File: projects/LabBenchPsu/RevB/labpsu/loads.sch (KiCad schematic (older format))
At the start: 33 parts

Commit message: schematic more or less done
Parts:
- removed 100n: C, symbol C
- removed C?: 1uF, symbol C
- removed IC?: OPAMP-DUALU, SparkFun-SO08, symbol OPAMP-DUALU
- removed U?: MCP3204, symbol MCP3204
- added C19, C22, C31: 100n, symbol C
- added unit 1 of IC3
- IC2, IC3: renamed from IC?; footprint SparkFun-SO08 -> (none)
- gave numbers to parts that had none: 26
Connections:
- net 3V3Reg: now also IC2.8 (V+), C19.2, C22.2, IC3.8 (V+)
- net GND: now also IC2.4 (V-), C19.1, C22.1, C31.1, IC3.4 (V-)
- net at IC2.3 (+IN), U8.1 (VOUT): now also C31.2
- net at Q1.2 (S), R33.1, R34.1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: now also IC3.5 (+IN); no longer IC2.5 (+IN)
- net at C21.2, R42.2, R43.2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: now also IC3.3 (+IN); no longer IC3.5 (+IN)
- removed net I_LOAD: C23.2, IC2.6 (-IN), IC2.7 (OUT)
- net V_LOAD renamed I_Load
- net I_Load: now also C23.2; no longer C24.2
- new net V_Load: C24.2, IC3.1 (OUT), IC3.2 (-IN)
- no-connect marks 4 -> 3
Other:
- note added: "I_Load: \n0-2A => 0-2V"
- note added: "SetCurrent: \n0-2V => 0-2A"
- note added: "V_Load: \n0-20V => 0-2V"
- note removed: "0-2.048 V"
- note removed: "ReadVolt: 1V = 10V"
- note removed: "SetCurrent: 1V = 1A"
- moved on the sheet: C20, C24, IC2A, IC2B, IC3B, JP3, JP4, Q1, R31, R32, R35, U8

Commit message: schematic with new DAC
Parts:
- removed C22: 100n, symbol C
- removed IC2, IC3: LM324, symbol OPAMP-DUALU
- removed U8: MCP4725, symbol MCP4725
- added P10: Heatsink, symbol CONN_2
- added U11: LM324N, symbol LM324N
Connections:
- net 3V3Reg: now also U11.4 (V+)
- net GND: now also U11.11 (V-); no longer C31.1
- net I_Load: now also U11.8, U11.9 (-)
- net SetCurrent: now also C31.1, U11.5 (+)
- net V_Load: now also U11.13 (-), U11.14
- net at C31.2: now also U11.4 (V+)
- net at C20.1, R35.2: now also U11.7
- net at C20.2, R36.2: now also U11.6 (-)
- net at Q1.2 (S), R33.1, R34.1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: now also U11.10 (+)
- net at C21.2, R42.2, R43.2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: now also U11.12 (+)
- no-connect marks 3 -> 5
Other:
- note added: "Voltage divider (/10) \nand lowpass filter"
- moved on the sheet: C19, C20, C21, C23, C24, C31, JP3, JP4, P8, Q1, R31, R32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

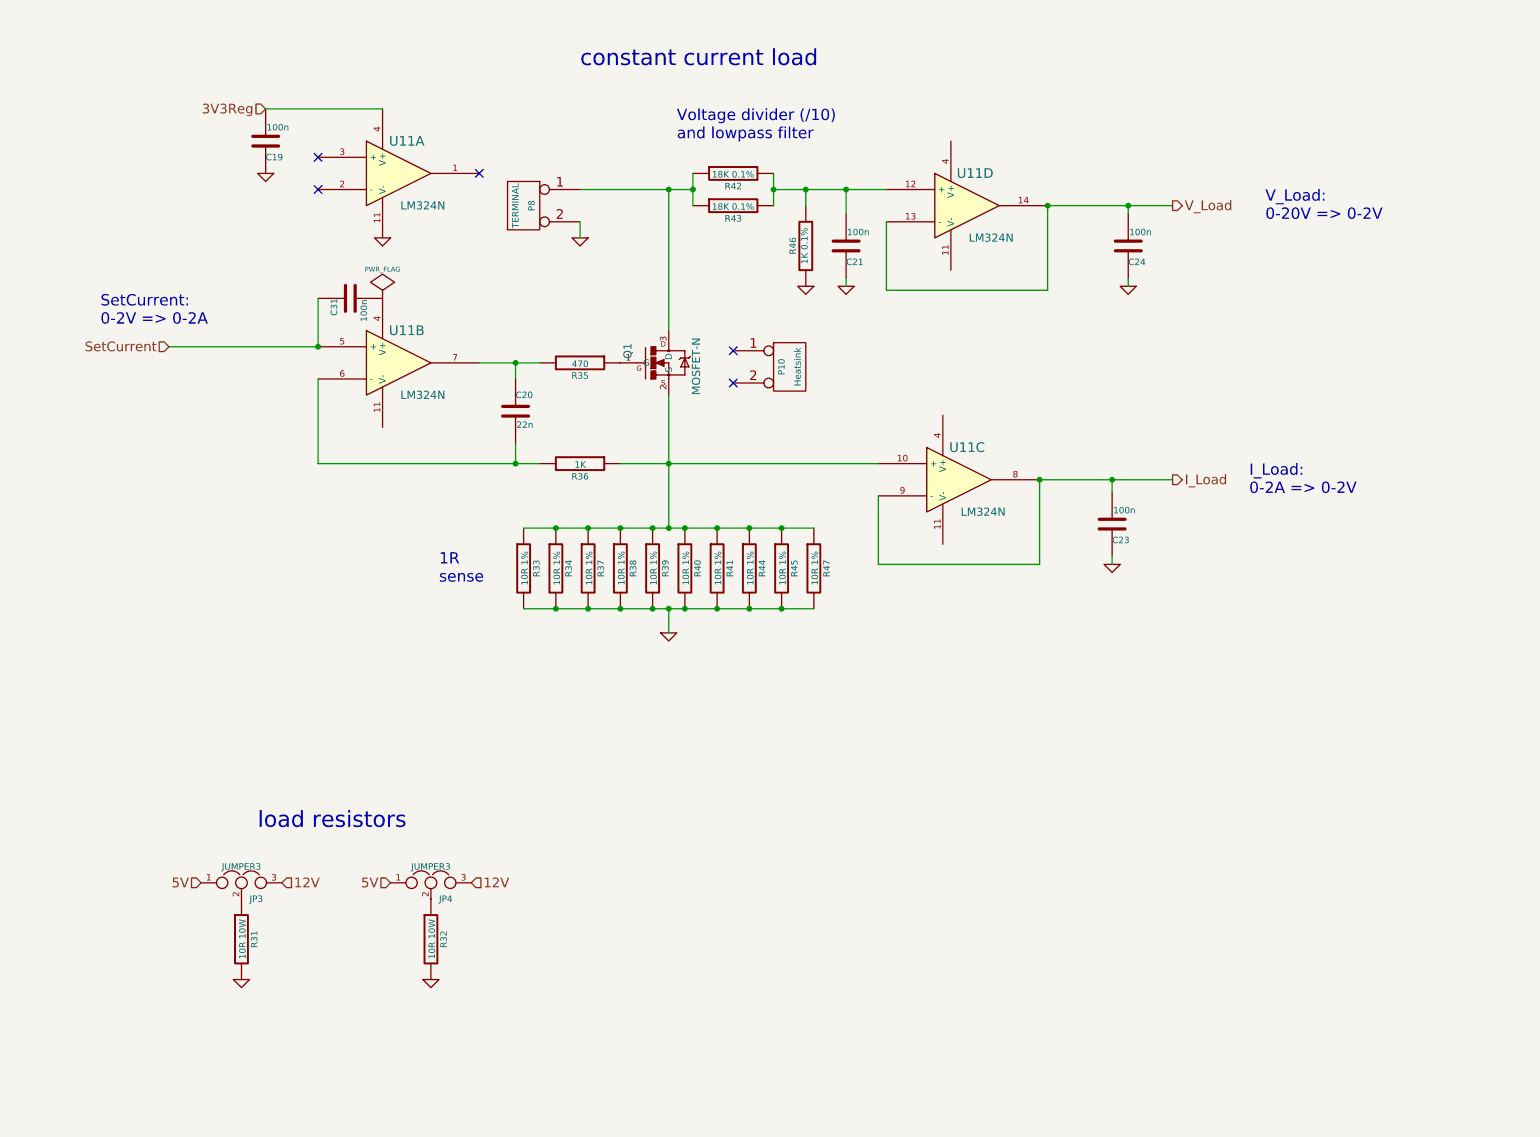
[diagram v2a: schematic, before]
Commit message: i2c addresses added
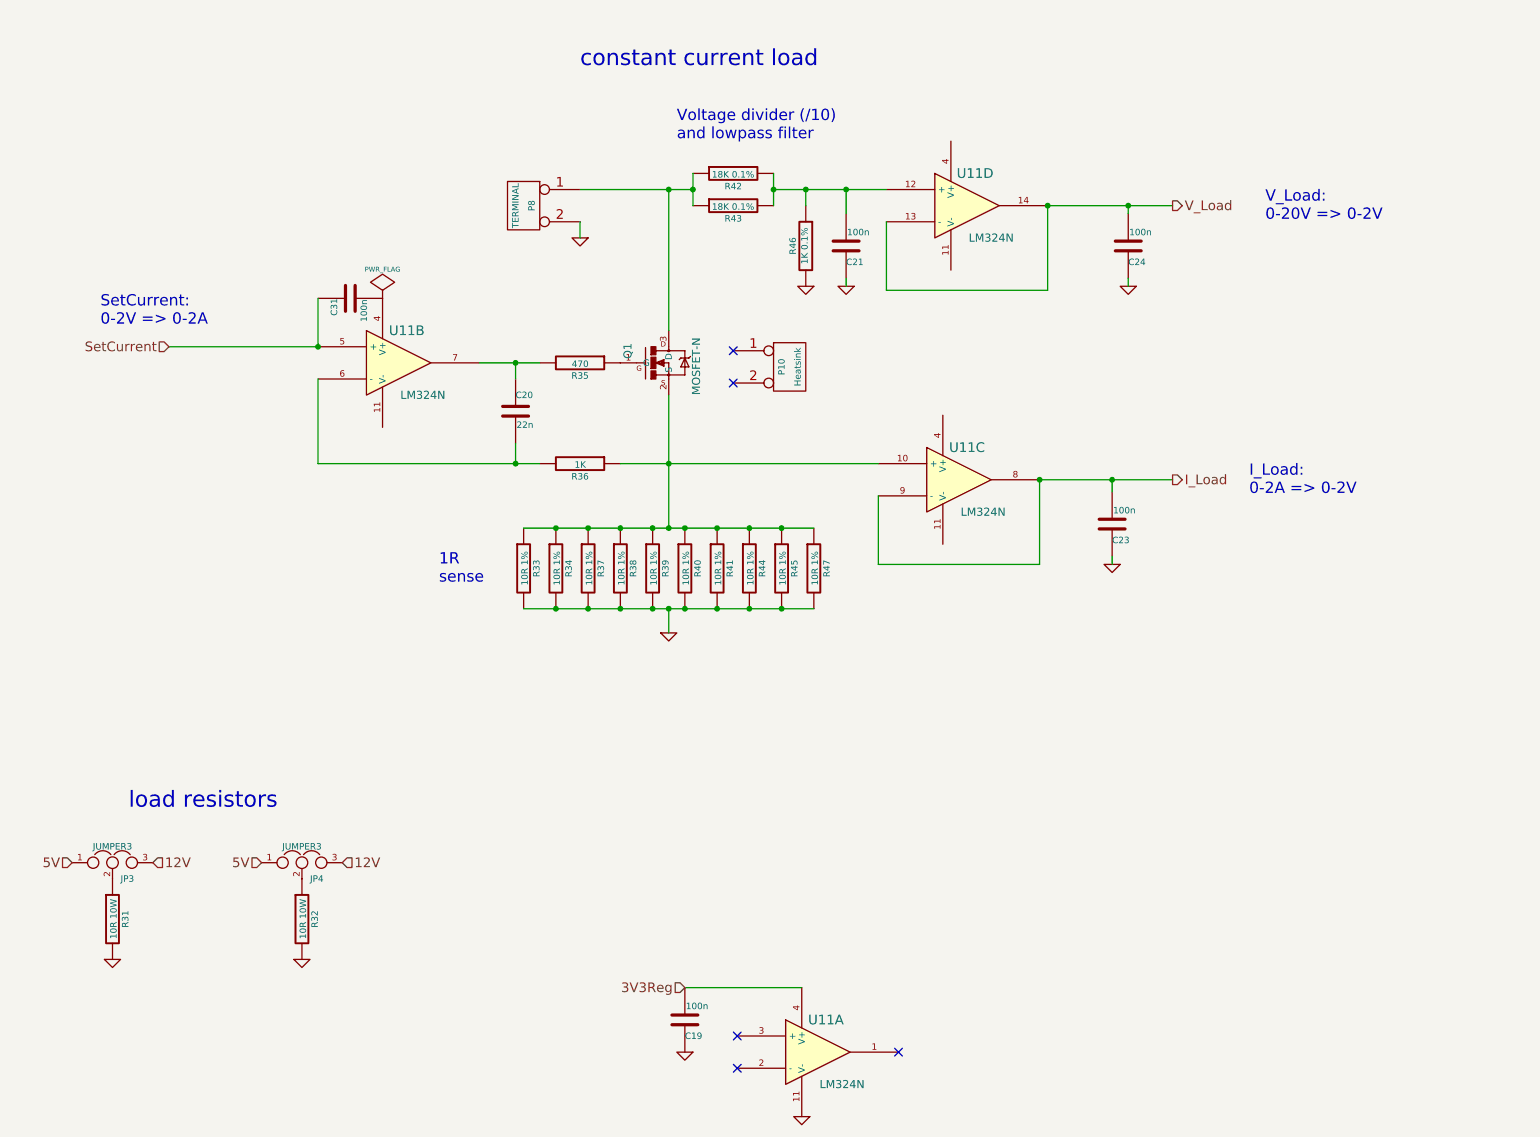
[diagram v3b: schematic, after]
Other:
- moved on the sheet: C19, JP3, JP4, R31, R32, U11A
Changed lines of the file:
@@
 L R R31
 U 1 1 57E1C01A
-P 2625 6450
-F 0 "R31" V 2705 6450 40  0000 C CNN
-F 1 "10R 10W" V 2632 6451 40  0000 C CNN
-F 2 "" V 2555 6450 30  0001 C CNN
-F 3 "" H 2625 6450 30  0000 C CNN
-	1    2625 6450
+P 1825 6325
+F 0 "R31" V 1905 6325 40  0000 C CNN
+F 1 "10R 10W" V 1832 6326 40  0000 C CNN
+F 2 "" V 1755 6325 30  0001 C CNN
+F 3 "" H 1825 6325 30  0000 C CNN
+	1    1825 6325
 	1    0    0    -1
 $EndComp
@@
 L JUMPER3 JP3
 U 1 1 57E1C059
-P 2625 6100
-F 0 "JP3" H 2675 6000 40  0000 L CNN
-F 1 "JUMPER3" H 2625 6200 40  0000 C CNN
-F 2 "" H 2625 6100 60  0001 C CNN
-F 3 "" H 2625 6100 60  0000 C CNN
-	1    2625 6100
+P 1825 5975
+F 0 "JP3" H 1875 5875 40  0000 L CNN
+F 1 "JUMPER3" H 1825 6075 40  0000 C CNN
+F 2 "" H 1825 5975 60  0001 C CNN
+F 3 "" H 1825 5975 60  0000 C CNN
+	1    1825 5975
 	1    0    0    -1
 $EndComp
@@
 L GND #PWR046
 U 1 1 57E1C08E
-P 2625 6700
-F 0 "#PWR046" H 2625 6700 30  0001 C CNN
-F 1 "GND" H 2625 6630 30  0001 C CNN
-F 2 "" H 2625 6700 60  0000 C CNN
-F 3 "" H 2625 6700 60  0000 C CNN
-	1    2625 6700
+P 1825 6575
+F 0 "#PWR046" H 1825 6575 30  0001 C CNN
+F 1 "GND" H 1825 6505 30  0001 C CNN
+F 2 "" H 1825 6575 60  0000 C CNN
+F 3 "" H 1825 6575 60  0000 C CNN
+	1    1825 6575
 	1    0    0    -1
 $EndComp
@@
 L R R32
 U 1 1 57E1C1C8
-P 3800 6450
-F 0 "R32" V 3880 6450 40  0000 C CNN
-F 1 "10R 10W" V 3807 6451 40  0000 C CNN
-F 2 "" V 3730 6450 30  0001 C CNN
-F 3 "" H 3800 6450 30  0000 C CNN
-	1    3800 6450
+P 3000 6325
+F 0 "R32" V 3080 6325 40  0000 C CNN
+F 1 "10R 10W" V 3007 6326 40  0000 C CNN
+F 2 "" V 2930 6325 30  0001 C CNN
+F 3 "" H 3000 6325 30  0000 C CNN
+	1    3000 6325
 	1    0    0    -1
 $EndComp
@@
 L JUMPER3 JP4
 U 1 1 57E1C1CF
-P 3800 6100
-F 0 "JP4" H 3850 6000 40  0000 L CNN
-F 1 "JUMPER3" H 3800 6200 40  0000 C CNN
-F 2 "" H 3800 6100 60  0001 C CNN
-F 3 "" H 3800 6100 60  0000 C CNN
-	1    3800 6100
+P 3000 5975
+F 0 "JP4" H 3050 5875 40  0000 L CNN
+F 1 "JUMPER3" H 3000 6075 40  0000 C CNN
+F 2 "" H 3000 5975 60  0001 C CNN
+F 3 "" H 3000 5975 60  0000 C CNN
+	1    3000 5975
 	1    0    0    -1
 $EndComp
@@
 L GND #PWR047
 U 1 1 57E1C1D6
-P 3800 6700
-F 0 "#PWR047" H 3800 6700 30  0001 C CNN
-F 1 "GND" H 3800 6630 30  0001 C CNN
-F 2 "" H 3800 6700 60  0000 C CNN
-F 3 "" H 3800 6700 60  0000 C CNN
-	1    3800 6700
-	1    0    0    -1
-$EndComp
-Text Notes 2725 5775 0    100  ~ 0
+P 3000 6575
+F 0 "#PWR047" H 3000 6575 30  0001 C CNN
+F 1 "GND" H 3000 6505 30  0001 C CNN
+F 2 "" H 3000 6575 60  0000 C CNN
+F 3 "" H 3000 6575 60  0000 C CNN
+	1    3000 6575
+	1    0    0    -1
+$EndComp
+Text Notes 1925 5650 0    100  ~ 0
 load resistors
-Text HLabel 2375 6100 0    60   Input ~ 0
+Text HLabel 1575 5975 0    60   Input ~ 0
 5V
-Text HLabel 2875 6100 2    60   Input ~ 0
+Text HLabel 2075 5975 2    60   Input ~ 0
 12V
-Text HLabel 3550 6100 0    60   Input ~ 0
+Text HLabel 2750 5975 0    60   Input ~ 0
 5V
-Text HLabel 4050 6100 2    60   Input ~ 0
+Text HLabel 3250 5975 2    60   Input ~ 0
 12V
 Text Notes 4725 1050 0    100  ~ 0
@@
 L GND #PWR054
 U 1 1 57F1092B
-P 3500 2100
-F 0 "#PWR054" H 3500 2100 30  0001 C CNN
-F 1 "GND" H 3500 2030 30  0001 C CNN
-F 2 "" H 3500 2100 60  0000 C CNN
-F 3 "" H 3500 2100 60  0000 C CNN
-	1    3500 2100
+P 6100 7550
+F 0 "#PWR054" H 6100 7550 30  0001 C CNN
+F 1 "GND" H 6100 7480 30  0001 C CNN
+F 2 "" H 6100 7550 60  0000 C CNN
+F 3 "" H 6100 7550 60  0000 C CNN
+	1    6100 7550
 	-1   0    0    -1
 $EndComp
@@
 L C C19
 U 1 1 57F10CA8
-P 2775 1500
-F 0 "C19" H 2775 1600 40  0000 L CNN
-F 1 "100n" H 2781 1415 40  0000 L CNN
-F 2 "" H 2813 1350 30  0001 C CNN
-F 3 "" H 2775 1500 60  0000 C CNN
-	1    2775 1500
+P 5375 6950
+F 0 "C19" H 5375 7050 40  0000 L CNN
+F 1 "100n" H 5381 6865 40  0000 L CNN
+F 2 "" H 5413 6800 30  0001 C CNN
+F 3 "" H 5375 6950 60  0000 C CNN
+	1    5375 6950
 	1    0    0    1
 $EndComp
@@
 L GND #PWR055
 U 1 1 57F1182D
-P 2775 1700
-F 0 "#PWR055" H 2775 1700 30  0001 C CNN
-F 1 "GND" H 2775 1630 30  0001 C CNN
-F 2 "" H 2775 1700 60  0000 C CNN
-F 3 "" H 2775 1700 60  0000 C CNN
-	1    2775 1700
-	-1   0    0    -1
-$EndComp
-Text HLabel 2775 1300 0    60   Input ~ 0
+P 5375 7150
+F 0 "#PWR055" H 5375 7150 30  0001 C CNN
+F 1 "GND" H 5375 7080 30  0001 C CNN
+F 2 "" H 5375 7150 60  0000 C CNN
+F 3 "" H 5375 7150 60  0000 C CNN
+	1    5375 7150
+	-1   0    0    -1
+$EndComp
+Text HLabel 5375 6750 0    60   Input ~ 0
 3V3Reg
 Wire Wire Line
@@
 L LM324N U11
 U 1 1 581E1824
-P 3600 1700
-F 0 "U11" H 3650 1900 60  0000 C CNN
-F 1 "LM324N" H 3750 1500 50  0000 C CNN
-F 2 "" H 3600 1700 60  0001 C CNN
-F 3 "" H 3600 1700 60  0000 C CNN
-	1    3600 1700
-	1    0    0    -1
-$EndComp
-NoConn ~ 4100 1700
-NoConn ~ 3100 1800
-NoConn ~ 3100 1600
-Wire Wire Line
-	3500 1300 2775 1300
+P 6200 7150
+F 0 "U11" H 6250 7350 60  0000 C CNN
+F 1 "LM324N" H 6350 6950 50  0000 C CNN
+F 2 "" H 6200 7150 60  0001 C CNN
+F 3 "" H 6200 7150 60  0000 C CNN
+	1    6200 7150
+	1    0    0    -1
+$EndComp
+NoConn ~ 6700 7150
+NoConn ~ 5700 7250
+NoConn ~ 5700 7050
+Wire Wire Line
+	6100 6750 5375 6750
 Wire Wire Line
 	3100 2975 3100 3500

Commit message: sepic calculations added
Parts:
- JP3, JP4: footprint (none) -> frep:Pin_Proto_Straight_1x03
- P8: footprint (none) -> frep:terminal_3p5mm_2pin
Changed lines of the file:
@@
 F 0 "JP3" H 1875 5875 40  0000 L CNN
 F 1 "JUMPER3" H 1825 6075 40  0000 C CNN
-F 2 "" H 1825 5975 60  0001 C CNN
+F 2 "frep:Pin_Proto_Straight_1x03" H 1825 5975 60  0001 C CNN
 F 3 "" H 1825 5975 60  0000 C CNN
 	1    1825 5975
@@
 F 0 "JP4" H 3050 5875 40  0000 L CNN
 F 1 "JUMPER3" H 3000 6075 40  0000 C CNN
-F 2 "" H 3000 5975 60  0001 C CNN
+F 2 "frep:Pin_Proto_Straight_1x03" H 3000 5975 60  0001 C CNN
 F 3 "" H 3000 5975 60  0000 C CNN
 	1    3000 5975
@@
 F 0 "P8" V 4325 1900 40  0000 C CNN
 F 1 "TERMINAL" V 4425 1900 40  0000 C CNN
-F 2 "" H 4375 1900 60  0001 C CNN
+F 2 "frep:terminal_3p5mm_2pin" H 4375 1900 60  0001 C CNN
 F 3 "" H 4375 1900 60  0000 C CNN
 	1    4375 1900
